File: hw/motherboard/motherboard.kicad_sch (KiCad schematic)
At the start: 3 parts

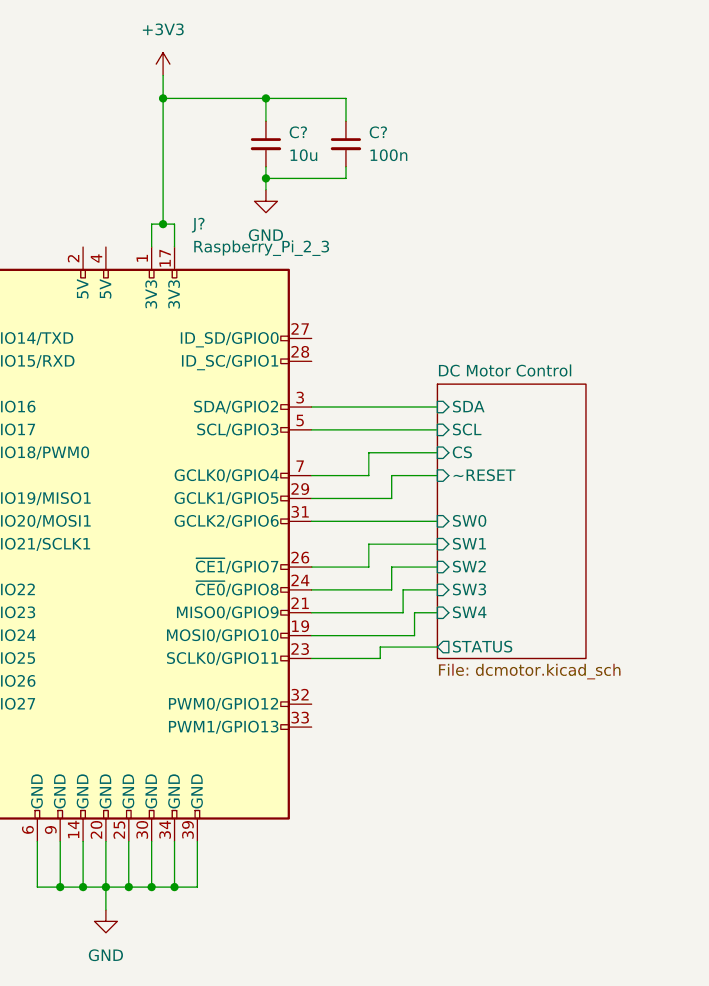
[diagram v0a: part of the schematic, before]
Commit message: Added LEDs and annotation.
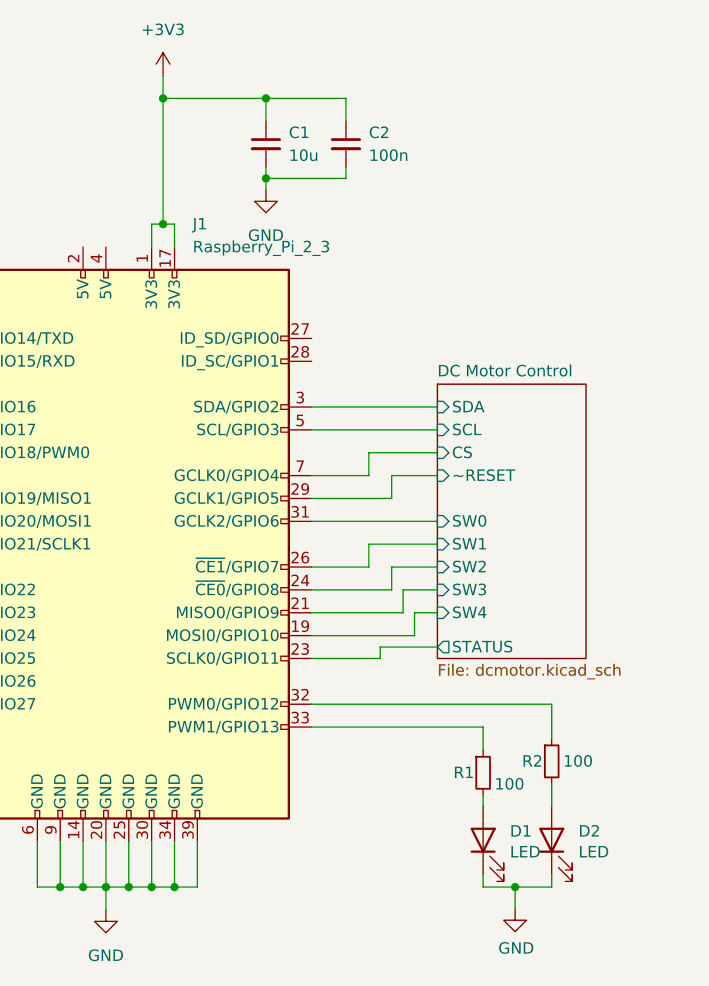
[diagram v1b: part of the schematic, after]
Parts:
- added D1, D2: LED, Diode_SMD:D_1206_3216Metric, symbol Device:LED
- added R1, R2: 100, Resistor_SMD:R_0805_2012Metric, symbol Device:R_Small
- gave numbers to parts that had none: 3
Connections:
- net GND: now also D1.1 (K), D2.1 (K)
- net at J1.32 (PWM0/GPIO12): now also R2.1
- net at J1.33 (PWM1/GPIO13): now also R1.1
- new net: D1.2 (A), R1.2
- new net: D2.2 (A), R2.2

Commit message: Added user interface to schematics.
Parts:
- removed D1, D2: LED, Diode_SMD:D_1206_3216Metric, symbol Device:LED
- removed R1, R2: 100, Resistor_SMD:R_0805_2012Metric, symbol Device:R_Small
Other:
- added sheet User Interface (ui.kicad_sch)

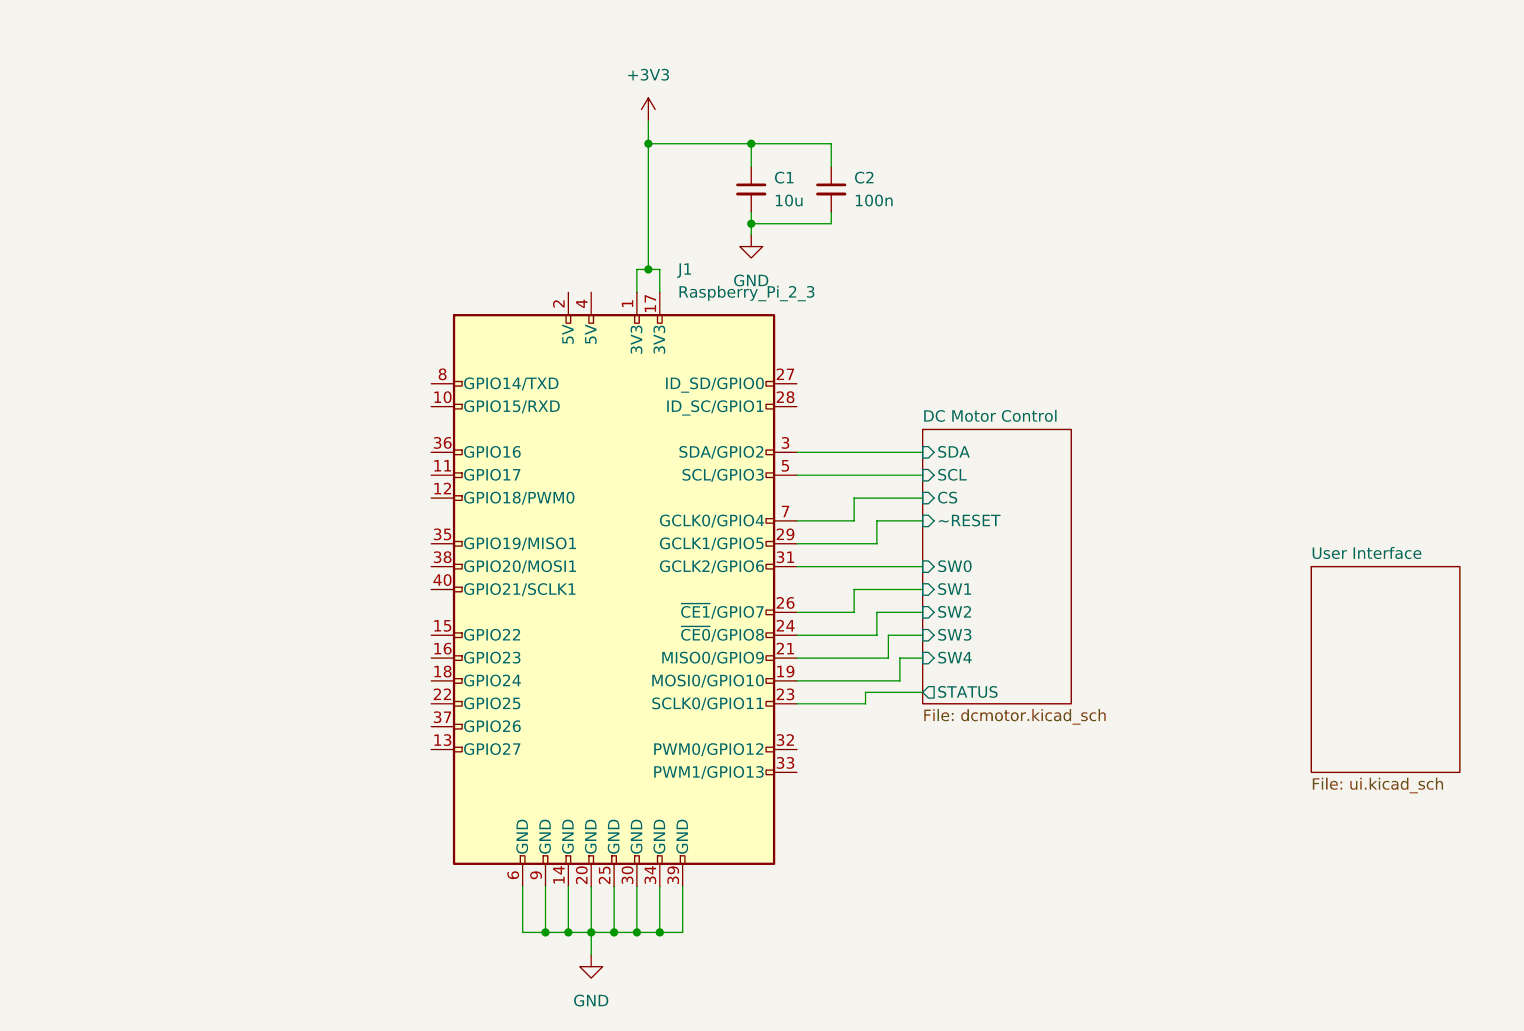
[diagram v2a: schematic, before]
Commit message: Added not used header.
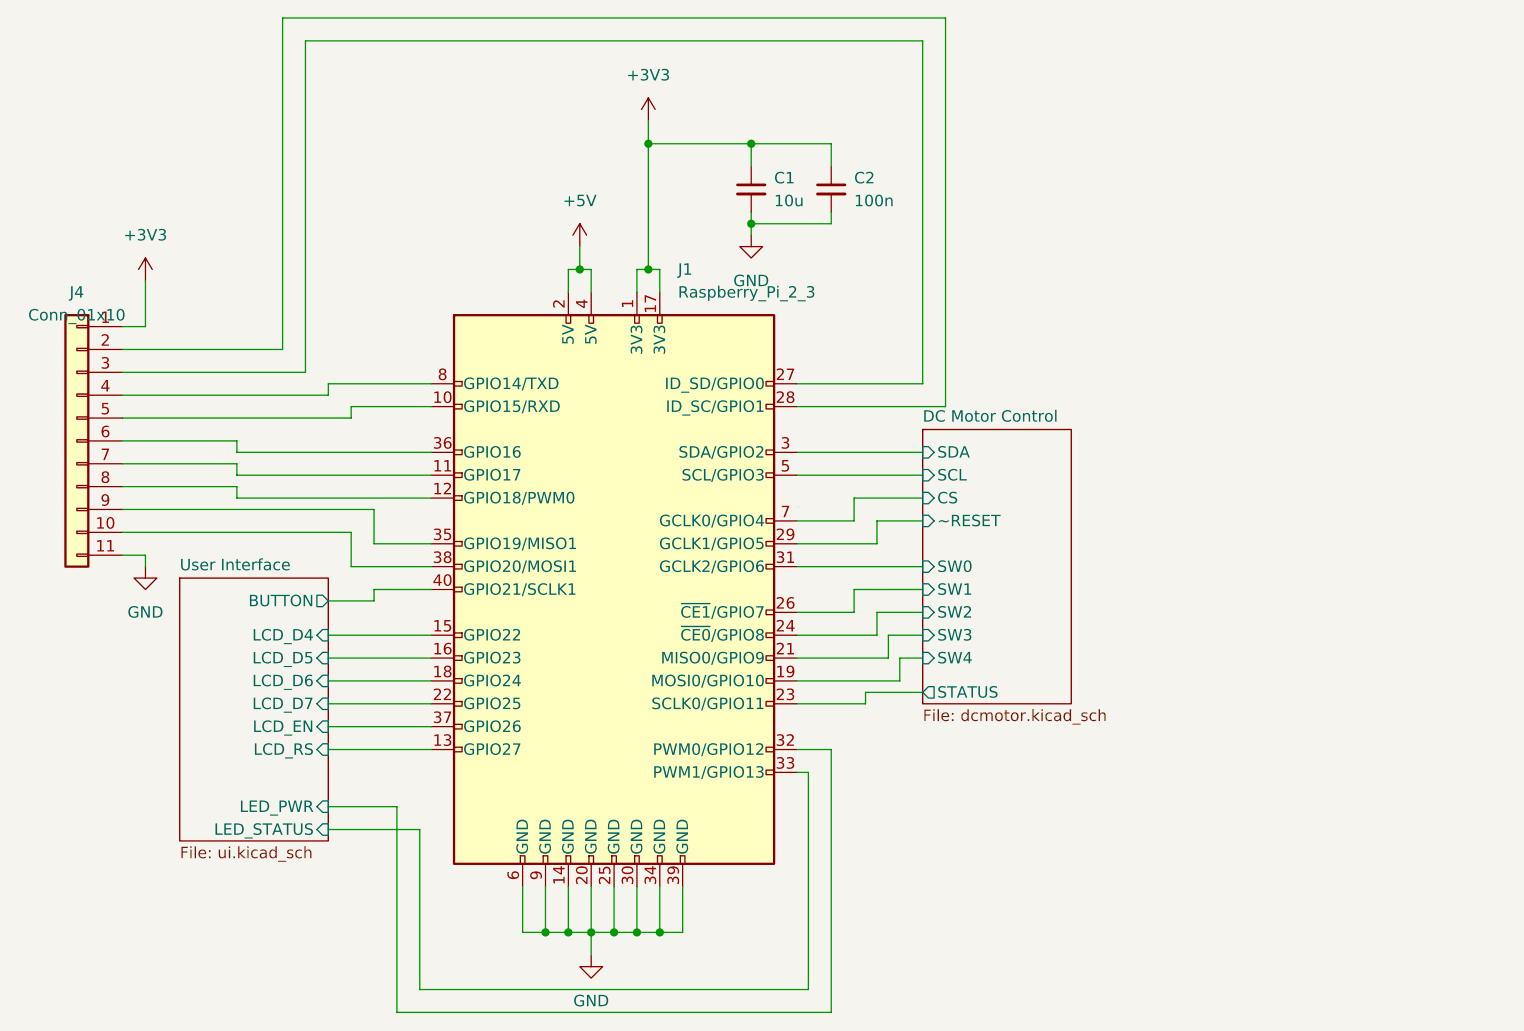
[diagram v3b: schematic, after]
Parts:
- added J4: Conn_01x10, symbol Connector_Generic:Conn_01x11
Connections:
- net +3V3: now also J4.1 (Pin_1)
- net GND: now also J4.11 (Pin_11)
- net at J1.10 (GPIO15/RXD): now also J4.5 (Pin_5)
- net at J1.11 (GPIO17): now also J4.7 (Pin_7)
- net at J1.12 (GPIO18/PWM0): now also J4.8 (Pin_8)
- net User Interface/LCD_RS: now reaches J1.13 (GPIO27)
- net User Interface/LCD_D4: now reaches J1.15 (GPIO22)
- net User Interface/LCD_D5: now reaches J1.16 (GPIO23)
- net User Interface/LCD_D6: now reaches J1.18 (GPIO24)
- net +5V: now reaches J1.2 (5V)
- net +5V: now also J1.4 (5V)
- net User Interface/LCD_D7: now reaches J1.22 (GPIO25)
- net at J1.27 (ID_SD/GPIO0): now also J4.3 (Pin_3)
- net at J1.28 (ID_SC/GPIO1): now also J4.2 (Pin_2)
- net User Interface/LED_PWR: now reaches J1.32 (PWM0/GPIO12)
- net User Interface/LED_STATUS: now reaches J1.33 (PWM1/GPIO13)
- net at J1.35 (GPIO19/MISO1): now also J4.9 (Pin_9)
- net at J1.36 (GPIO16): now also J4.6 (Pin_6)
- net User Interface/LCD_EN: now reaches J1.37 (GPIO26)
- net at J1.38 (GPIO20/MOSI1): now also J4.10 (Pin_10)
- net User Interface/BUTTON: now reaches J1.40 (GPIO21/SCLK1)
- net at J1.8 (GPIO14/TXD): now also J4.4 (Pin_4)
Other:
- sheet User Interface ports: added BUTTON, LCD_D4, LCD_D5, LCD_D6, LCD_D7, LCD_EN, LCD_RS, LED_PWR, LED_STATUS; removed none

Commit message: Fixed DRC errors on schematic
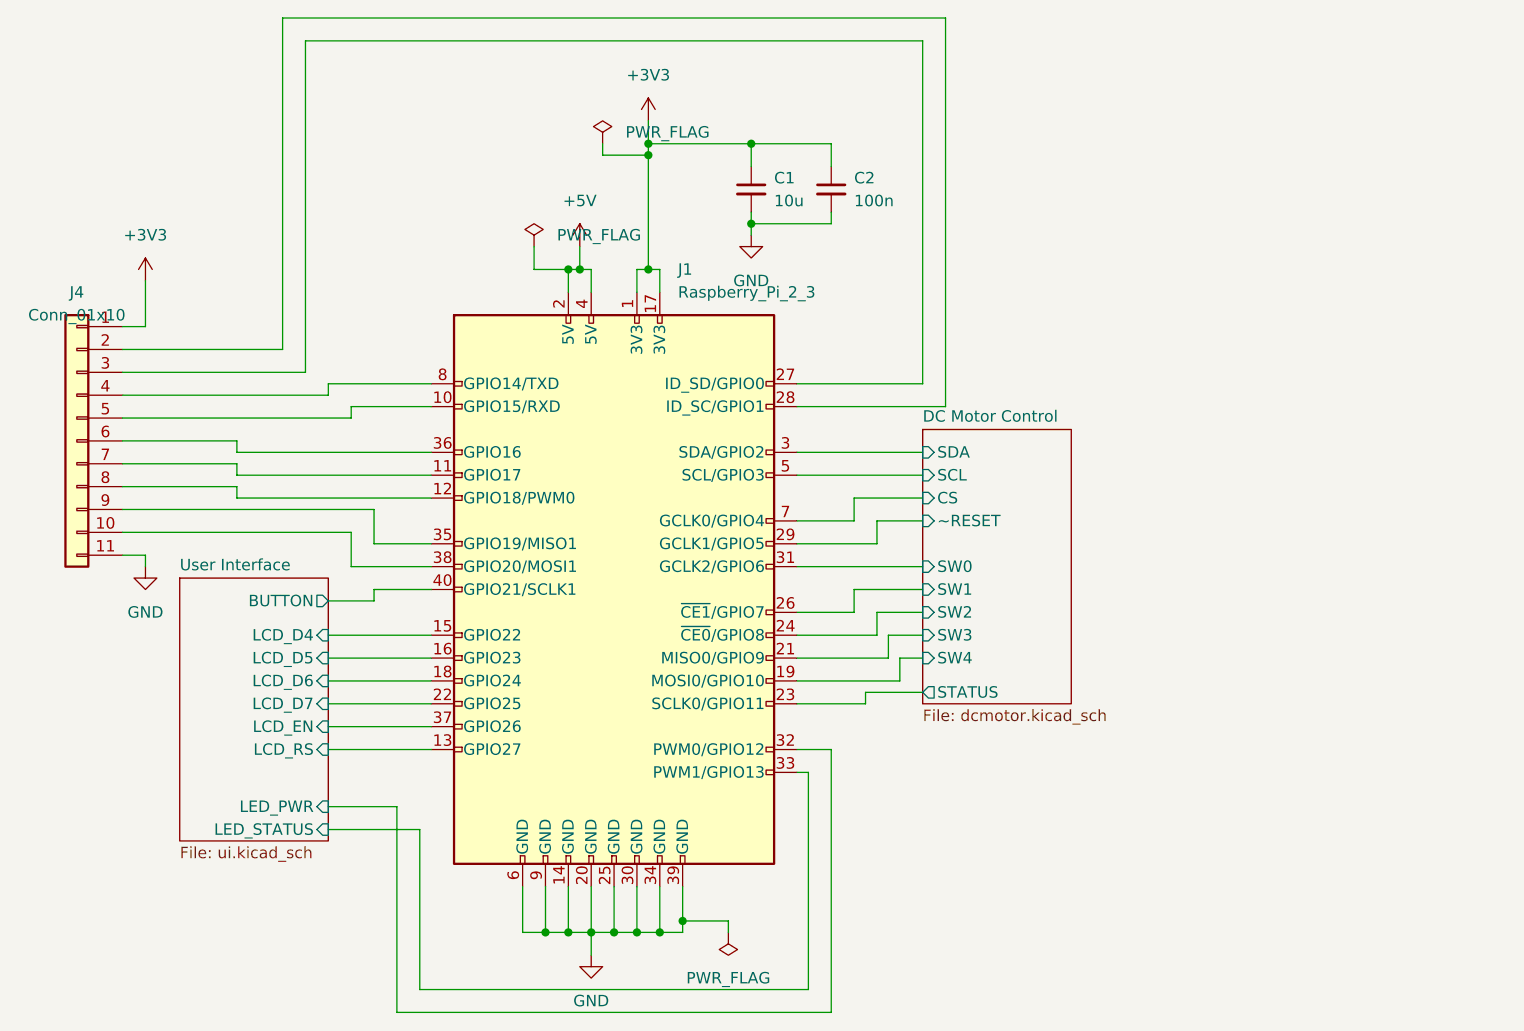
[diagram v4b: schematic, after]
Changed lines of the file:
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@@
   (junction (at 129.54 54.61) (diameter 0) (color 0 0 0 0)
   )
+  (junction (at 109.22 59.69) (diameter 0) (color 0 0 0 0)
+  )
+  (junction (at 118.11 46.99) (diameter 0) (color 0 0 0 0)
+  )
   (junction (at 109.22 133.35) (diameter 0) (color 0 0 0 0)
   )
   (junction (at 118.11 45.72) (diameter 0) (color 0 0 0 0)
   )
+  (junction (at 121.92 132.08) (diameter 0) (color 0 0 0 0)
+  )
   (junction (at 110.49 59.69) (diameter 0) (color 0 0 0 0)
   )
@@
     (stroke (width 0) (type default) (color 0 0 0 0))
   )
-  (wire (pts (xy 121.92 133.35) (xy 121.92 128.27))
+  (wire (pts (xy 127 133.35) (xy 127 132.08))
+    (stroke (width 0) (type default) (color 0 0 0 0))
+  )
+  (wire (pts (xy 105.41 59.69) (xy 109.22 59.69))
+    (stroke (width 0) (type default) (color 0 0 0 0))
+  )
+  (wire (pts (xy 121.92 133.35) (xy 121.92 132.08))
     (stroke (width 0) (type default) (color 0 0 0 0))
   )
@@
     (stroke (width 0) (type default) (color 0 0 0 0))
   )
+  (wire (pts (xy 121.92 132.08) (xy 121.92 128.27))
+    (stroke (width 0) (type default) (color 0 0 0 0))
+  )
+  (wire (pts (xy 127 132.08) (xy 121.92 132.08))
+    (stroke (width 0) (type default) (color 0 0 0 0))
+  )
   (wire (pts (xy 146.05 102.87) (xy 146.05 105.41))
     (stroke (width 0) (type default) (color 0 0 0 0))
@@
     (stroke (width 0) (type default) (color 0 0 0 0))
   )
+  (wire (pts (xy 113.03 46.99) (xy 118.11 46.99))
+    (stroke (width 0) (type default) (color 0 0 0 0))
+  )
+  (wire (pts (xy 118.11 46.99) (xy 118.11 59.69))
+    (stroke (width 0) (type default) (color 0 0 0 0))
+  )
   (wire (pts (xy 59.69 71.12) (xy 80.01 71.12))
     (stroke (width 0) (type default) (color 0 0 0 0))
@@
     (stroke (width 0) (type default) (color 0 0 0 0))
   )
-  (wire (pts (xy 118.11 45.72) (xy 118.11 59.69))
+  (wire (pts (xy 118.11 45.72) (xy 118.11 46.99))
     (stroke (width 0) (type default) (color 0 0 0 0))
   )
@@
     (stroke (width 0) (type default) (color 0 0 0 0))
   )
+  (wire (pts (xy 113.03 45.72) (xy 113.03 46.99))
+    (stroke (width 0) (type default) (color 0 0 0 0))
+  )
   (wire (pts (xy 151.13 31.75) (xy 77.47 31.75))
     (stroke (width 0) (type default) (color 0 0 0 0))
@@
   )
   (wire (pts (xy 148.59 97.79) (xy 143.51 97.79))
+    (stroke (width 0) (type default) (color 0 0 0 0))
+  )
+  (wire (pts (xy 105.41 57.15) (xy 105.41 59.69))
     (stroke (width 0) (type default) (color 0 0 0 0))
   )
@@
     (pin "9")
   )
+  (symbol (lib_id "power:PWR_FLAG") (at 113.03 45.72 0) (unit 1)
+    (in_bom yes) (on_board yes) (fields_autoplaced)
+    (property "Reference" "#FLG0103" (id 0) (at 113.03 43.815 0)
+      (effects (font (size 1.27 1.27)) hide)
+    )
+    (property "Value" "PWR_FLAG" (id 1) (at 115.57 44.4499 0)
+      (effects (font (size 1.27 1.27)) (justify left))
+    )
+    (property "Footprint" "" (id 2) (at 113.03 45.72 0)
+      (effects (font (size 1.27 1.27)) hide)
+    )
+    (property "Datasheet" "~" (id 3) (at 113.03 45.72 0)
+      (effects (font (size 1.27 1.27)) hide)
+    )
+    (pin "1")
+  )
   (symbol (lib_id "power:+5V") (at 110.49 57.15 0) (unit 1)
     (in_bom yes) (on_board yes) (fields_autoplaced)
@@
     (pin "1")
   )
+  (symbol (lib_id "power:PWR_FLAG") (at 127 133.35 180) (unit 1)
+    (in_bom yes) (on_board yes) (fields_autoplaced)
+    (property "Reference" "#FLG0101" (id 0) (at 127 135.255 0)
+      (effects (font (size 1.27 1.27)) hide)
+    )
+    (property "Value" "PWR_FLAG" (id 1) (at 127 138.43 0))
+    (property "Footprint" "" (id 2) (at 127 133.35 0)
+      (effects (font (size 1.27 1.27)) hide)
+    )
+    (property "Datasheet" "~" (id 3) (at 127 133.35 0)
+      (effects (font (size 1.27 1.27)) hide)
+    )
+    (pin "1")
+  )
   (symbol (lib_id "Device:C_Small") (at 129.54 50.8 0) (unit 1)
     (in_bom yes) (on_board yes) (fields_autoplaced)
@@
     )
     (property "Datasheet" "" (id 3) (at 62.23 92.71 0)
+      (effects (font (size 1.27 1.27)) hide)
+    )
+    (pin "1")
+  )
+  (symbol (lib_id "power:PWR_FLAG") (at 105.41 57.15 0) (unit 1)
+    (in_bom yes) (on_board yes) (fields_autoplaced)
+    (property "Reference" "#FLG0102" (id 0) (at 105.41 55.245 0)
+      (effects (font (size 1.27 1.27)) hide)
+    )
+    (property "Value" "PWR_FLAG" (id 1) (at 107.95 55.8799 0)
+      (effects (font (size 1.27 1.27)) (justify left))
+    )
+    (property "Footprint" "" (id 2) (at 105.41 57.15 0)
+      (effects (font (size 1.27 1.27)) hide)
+    )
+    (property "Datasheet" "~" (id 3) (at 105.41 57.15 0)
       (effects (font (size 1.27 1.27)) hide)
     )
@@
   )
   (symbol_instances
+    (path "/b9d7e89a-05d8-4f77-8429-00cc5b5ce698"
+      (reference "#FLG0101") (unit 1) (value "PWR_FLAG") (footprint "")
+    )
+    (path "/de2f08ac-bd0c-47a8-804f-322f50d7f2c5"
+      (reference "#FLG0102") (unit 1) (value "PWR_FLAG") (footprint "")
+    )
+    (path "/67404a98-a318-4575-8be7-459933080f0f"
+      (reference "#FLG0103") (unit 1) (value "PWR_FLAG") (footprint "")
+    )
+    (path "/7eb79170-3bad-497b-ae6e-2ded53d67852/bc2cf87b-79c1-4376-80a3-24488ce09a21"
+      (reference "#FLG0104") (unit 1) (value "PWR_FLAG") (footprint "")
+    )
+    (path "/7eb79170-3bad-497b-ae6e-2ded53d67852/2433adc2-160f-49a3-ac1c-21769cc1c2f8"
+      (reference "#FLG0105") (unit 1) (value "PWR_FLAG") (footprint "")
+    )
     (path "/b645f9b2-a376-4c2d-8701-ba7b73243039"
       (reference "#PWR01") (unit 1) (value "GND") (footprint "")
